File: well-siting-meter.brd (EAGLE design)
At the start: 93.8 x 65.9 mm, 46 parts, among them J2 7805, T1 MOSFET-NCHANNELFQP30N06L, U1 LCD-16X2NOHOLES, U2 ARDUINO_PRO_MINI, U3 EC2, U4 EC2, U5 AD623, U6 AD623, U7 MAX1771

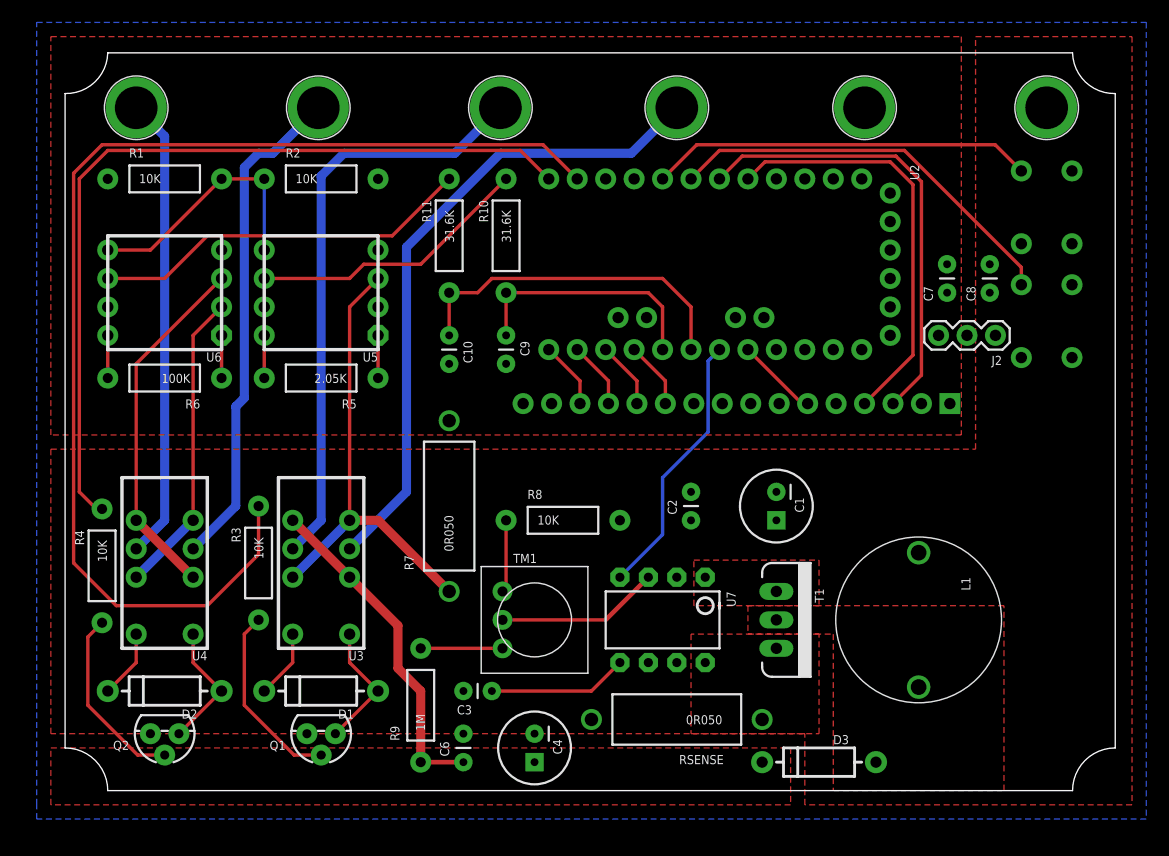
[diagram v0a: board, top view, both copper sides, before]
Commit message: adding optional 2nd inductor, more mfg prep
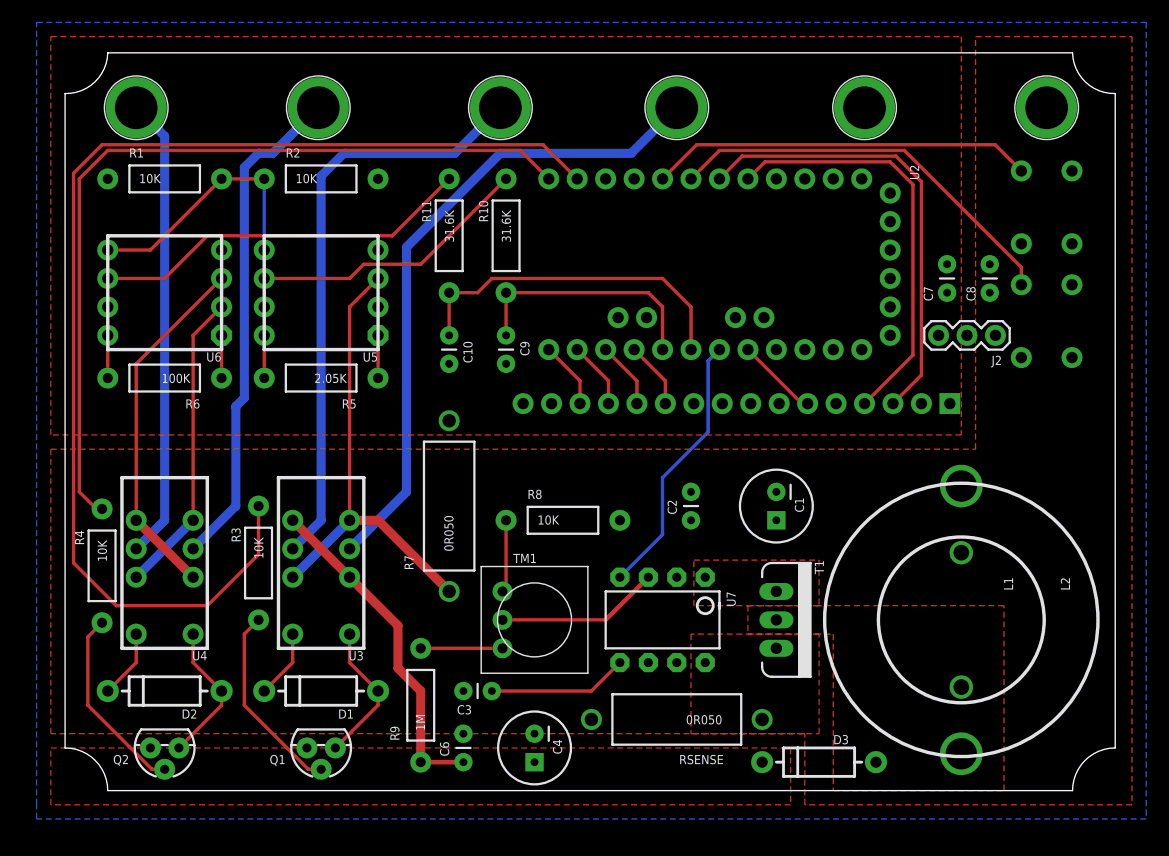
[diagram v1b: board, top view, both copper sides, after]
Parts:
- added L2: 47uH, murata1400:MURATA1400
- moved L1 3.81 mm to (81.3, 16.5)
- moved Q1 1.27 mm to (24.1, 5.08)
- moved Q2 1.27 mm to (10.2, 5.08)
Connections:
- net N$9: now also L2.P$2
- net V_BATT: now also L2.P$1
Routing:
- net N$4: track 11.5 -> 12.8 mm
- net N$1: track 11.5 -> 12.8 mm
- net N$5: track 16.8 -> 17.4 mm
- net N$2: track 16.6 -> 17.1 mm
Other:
- board text added: "BATT"
- board text added: "danwahl.github.io/"
- board text added: "rev -"
- board text added: "sn:"
- board text added: "v2"
- board text removed: "VBAT"
- board text removed: "danwahl.net/"
- board text removed: "v2 | rev - | sn:"
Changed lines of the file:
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@@
 <wire x1="91.2114" y1="1.27" x2="95.0214" y2="5.08" width="0" layer="20" curve="-90"/>
 <wire x1="1.27" y1="5.08" x2="5.08" y2="1.27" width="0" layer="20" curve="-90"/>
-<text x="93.98" y="14.478" size="1.778" layer="51" font="vector" ratio="10" rot="R90">well-siting-meter</text>
-<text x="74.93" y="2.54" size="0.8128" layer="51" font="vector" ratio="10">v2 | rev - | sn:</text>
-<text x="93.98" y="6.35" size="0.8128" layer="51" font="vector" ratio="10" rot="R90">danwahl.net/</text>
-<rectangle x1="86.36" y1="1.27" x2="91.44" y2="5.08" layer="51"/>
-<text x="88.9" y="66.04" size="1.016" layer="51" font="vector" ratio="10" align="center">VBAT</text>
+<text x="93.98" y="21.59" size="1.4224" layer="51" font="vector" ratio="10" rot="R90">well-siting-meter</text>
+<text x="83.82" y="29.21" size="0.8128" layer="51" font="vector" ratio="10" rot="R90">v2</text>
+<text x="91.44" y="25.146" size="0.8128" layer="51" font="vector" ratio="10" rot="R90">danwahl.github.io/</text>
+<text x="88.9" y="66.04" size="1.016" layer="51" font="vector" ratio="10" align="center">BATT</text>
 <text x="72.644" y="66.04" size="1.016" layer="51" font="vector" ratio="10" align="center">GND</text>
 <text x="55.88" y="66.04" size="1.016" layer="52" font="vector" ratio="10" rot="MR0" align="center">I1</text>
@@
 <text x="23.876" y="66.04" size="1.016" layer="51" font="vector" ratio="10" align="center">V1</text>
 <text x="7.62" y="66.04" size="1.016" layer="51" font="vector" ratio="10" align="center">V2</text>
-<text x="88.9" y="66.04" size="1.016" layer="52" font="vector" ratio="10" rot="MR0" align="center">VBAT</text>
+<text x="88.9" y="66.04" size="1.016" layer="52" font="vector" ratio="10" rot="MR0" align="center">BATT</text>
 <text x="72.644" y="66.04" size="1.016" layer="52" font="vector" ratio="10" rot="MR0" align="center">GND</text>
 <text x="55.88" y="66.04" size="1.016" layer="51" font="vector" ratio="10" align="center">I1</text>
@@
 <text x="23.876" y="66.04" size="1.016" layer="52" font="vector" ratio="10" rot="MR0" align="center">V1</text>
 <text x="7.62" y="66.04" size="1.016" layer="52" font="vector" ratio="10" rot="MR0" align="center">V2</text>
+<text x="86.36" y="28.448" size="0.8128" layer="51" font="vector" ratio="10" rot="R90">rev -</text>
+<text x="88.9" y="26.924" size="0.8128" layer="51" font="vector" ratio="10" rot="R90">sn:</text>
+<rectangle x1="87.376" y1="29.21" x2="89.916" y2="34.29" layer="51"/>
 </plain>
 <attributes>
@@
 <attribute name="VALUE" x="15.24" y="52.07" size="0.8128" layer="27" font="vector" rot="R180"/>
 </element>
-<element name="Q1" library="SparkFun-DiscreteSemi" package="TO-92" value="" x="24.13" y="6.35" smashed="yes" rot="R180">
-<attribute name="PROD_ID" value="TRANS-09536" x="24.13" y="6.35" size="1.778" layer="27" rot="R180" display="off"/>
-<attribute name="PN" value="PN2222AFS-ND" x="24.13" y="6.35" size="1.778" layer="27" rot="R180" display="off"/>
-<attribute name="NAME" x="20.955" y="5.715" size="0.8128" layer="25" font="vector" ratio="10" rot="R180"/>
-<attribute name="VALUE" x="20.955" y="7.62" size="0.4064" layer="27" ratio="10" rot="R180"/>
-</element>
-<element name="Q2" library="SparkFun-DiscreteSemi" package="TO-92" value="" x="10.16" y="6.35" smashed="yes" rot="R180">
-<attribute name="PROD_ID" value="TRANS-09536" x="10.16" y="6.35" size="1.778" layer="27" rot="R180" display="off"/>
-<attribute name="PN" value="PN2222AFS-ND" x="10.16" y="6.35" size="1.778" layer="27" rot="R180" display="off"/>
-<attribute name="NAME" x="6.985" y="5.715" size="0.8128" layer="25" font="vector" ratio="10" rot="R180"/>
-<attribute name="VALUE" x="6.985" y="7.62" size="0.4064" layer="27" ratio="10" rot="R180"/>
+<element name="Q1" library="SparkFun-DiscreteSemi" package="TO-92" value="" x="24.13" y="5.08" smashed="yes" rot="R180">
+<attribute name="PROD_ID" value="TRANS-09536" x="24.13" y="5.08" size="1.778" layer="27" rot="R180" display="off"/>
+<attribute name="PN" value="PN2222AFS-ND" x="24.13" y="5.08" size="1.778" layer="27" rot="R180" display="off"/>
+<attribute name="NAME" x="20.955" y="4.445" size="0.8128" layer="25" font="vector" ratio="10" rot="R180"/>
+<attribute name="VALUE" x="20.955" y="6.35" size="0.4064" layer="27" ratio="10" rot="R180"/>
+</element>
+<element name="Q2" library="SparkFun-DiscreteSemi" package="TO-92" value="" x="10.16" y="5.08" smashed="yes" rot="R180">
+<attribute name="PROD_ID" value="TRANS-09536" x="10.16" y="5.08" size="1.778" layer="27" rot="R180" display="off"/>
+<attribute name="PN" value="PN2222AFS-ND" x="10.16" y="5.08" size="1.778" layer="27" rot="R180" display="off"/>
+<attribute name="NAME" x="6.985" y="4.445" size="0.8128" layer="25" font="vector" ratio="10" rot="R180"/>
+<attribute name="VALUE" x="6.985" y="6.35" size="0.4064" layer="27" ratio="10" rot="R180"/>
 </element>
 <element name="D1" library="SparkFun-DiscreteSemi" package="DIODE-1N4001" value="" x="24.13" y="10.16" smashed="yes" rot="R180">
@@
 <attribute name="PN" value="BC2665CT-ND" x="39.37" y="10.16" size="1.778" layer="27" rot="R180" display="off"/>
 <attribute name="NAME" x="37.592" y="8.89" size="0.8128" layer="25" font="vector" rot="R180"/>
-<attribute name="VALUE" x="39.116" y="12.192" size="0.8128" layer="27" font="vector" rot="R180"/>
+<attribute name="VALUE" x="37.846" y="12.192" size="0.8128" layer="27" font="vector" rot="R180"/>
 </element>
 <element name="T1" library="SparkFun-DiscreteSemi" package="TO220V" value="MOSFET-NCHANNELFQP30N06L" x="64.77" y="16.51" smashed="yes" rot="R270">
 <attribute name="PROD_ID" value="TRANS-10060" x="64.77" y="16.51" size="1.778" layer="27" rot="R270" display="off"/>
 <attribute name="PN" value="FDP33N25-ND" x="64.77" y="16.51" size="1.778" layer="27" rot="R270" display="off"/>
-<attribute name="NAME" x="68.199" y="19.304" size="0.8128" layer="25" font="vector" ratio="10" rot="R270"/>
+<attribute name="NAME" x="68.199" y="21.844" size="0.8128" layer="25" font="vector" ratio="10" rot="R270"/>
 </element>
 <element name="D3" library="SparkFun-DiscreteSemi" package="DIODE-1N4001" value="" x="68.58" y="3.81" smashed="yes" rot="R180">
@@
 <attribute name="VALUE" x="41.275" y="10.16" size="1.27" layer="27"/>
 </element>
-<element name="L1" library="misc" package="1415" value="22uH" x="77.47" y="16.51" smashed="yes" rot="R270">
-<attribute name="NAME" x="81.28" y="20.32" size="0.8128" layer="25" font="vector" rot="R270"/>
-<attribute name="VALUE" x="72.39" y="20.32" size="0.8128" layer="27" font="vector" rot="R270"/>
+<element name="L1" library="misc" package="1415" value="22uH" x="81.28" y="16.51" smashed="yes" rot="R270">
+<attribute name="NAME" x="85.09" y="20.32" size="0.8128" layer="25" font="vector" rot="R270"/>
+<attribute name="VALUE" x="76.2" y="20.32" size="0.8128" layer="27" font="vector" rot="R270"/>
+<attribute name="PN" value="732-7163-ND" x="81.28" y="16.51" size="1.778" layer="27" rot="R270" display="off"/>
+</element>
+<element name="L2" library="murata1400" package="MURATA1400" value="47uH" x="81.28" y="16.51" smashed="yes" rot="R270">
+<attribute name="NAME" x="90.17" y="20.32" size="0.8128" layer="25" font="vector" ratio="10" rot="R270"/>
+<attribute name="VALUE" x="71.12" y="20.32" size="0.8128" layer="27" font="vector" ratio="10" rot="R270"/>
+<attribute name="PN" value="811-2633-ND" x="81.28" y="16.51" size="1.778" layer="27" rot="R270" display="off"/>
 </element>
 </elements>
@@
 <wire x1="15.24" y1="10.16" x2="12.7" y2="12.7" width="0.3048" layer="1"/>
 <wire x1="12.7" y1="12.7" x2="12.7" y2="15.24" width="0.3048" layer="1"/>
-<wire x1="11.43" y1="6.35" x2="15.24" y2="10.16" width="0.3048" layer="1"/>
+<wire x1="15.24" y1="10.16" x2="15.24" y2="8.89" width="0.3048" layer="1"/>
+<wire x1="15.24" y1="8.89" x2="11.43" y2="5.08" width="0.3048" layer="1"/>
 </signal>
 <signal name="N$2">
@@
 <wire x1="4.572" y1="16.256" x2="3.302" y2="14.986" width="0.3048" layer="1"/>
 <wire x1="3.302" y1="14.986" x2="3.302" y2="8.89" width="0.3048" layer="1"/>
-<wire x1="3.302" y1="8.89" x2="7.747" y2="4.445" width="0.3048" layer="1"/>
-<wire x1="7.747" y1="4.445" x2="10.16" y2="4.445" width="0.3048" layer="1"/>
+<wire x1="10.16" y1="3.175" x2="9.017" y2="3.175" width="0.3048" layer="1"/>
+<wire x1="9.017" y1="3.175" x2="3.302" y2="8.89" width="0.3048" layer="1"/>
 </signal>
 <signal name="VSW">
@@
 <wire x1="29.21" y1="10.16" x2="26.67" y2="12.7" width="0.3048" layer="1"/>
 <wire x1="26.67" y1="12.7" x2="26.67" y2="15.24" width="0.3048" layer="1"/>
-<wire x1="25.4" y1="6.35" x2="29.21" y2="10.16" width="0.3048" layer="1"/>
+<wire x1="29.21" y1="10.16" x2="29.21" y2="8.89" width="0.3048" layer="1"/>
+<wire x1="29.21" y1="8.89" x2="25.4" y2="5.08" width="0.3048" layer="1"/>
 </signal>
 <signal name="N$5">
@@
 <wire x1="18.542" y1="16.51" x2="17.272" y2="15.24" width="0.3048" layer="1"/>
 <wire x1="17.272" y1="15.24" x2="17.272" y2="8.89" width="0.3048" layer="1"/>
-<wire x1="17.272" y1="8.89" x2="21.717" y2="4.445" width="0.3048" layer="1"/>
-<wire x1="21.717" y1="4.445" x2="24.13" y2="4.445" width="0.3048" layer="1"/>
+<wire x1="24.13" y1="3.175" x2="22.987" y2="3.175" width="0.3048" layer="1"/>
+<wire x1="22.987" y1="3.175" x2="17.272" y2="8.89" width="0.3048" layer="1"/>
 </signal>
 <signal name="ISW">
@@
 <contactref element="C2" pad="1"/>
 <contactref element="L1" pad="P1"/>
+<contactref element="L2" pad="P$1"/>
 </signal>
 <signal name="RS">
@@
 </polygon>
 <contactref element="L1" pad="P2"/>
+<contactref element="L2" pad="P$2"/>
 </signal>
 <signal name="N$10">

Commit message: fixed cap packages (5mm)
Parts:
- C10, C2, C3, C6, C7, C8, C9: device SparkFun-Passives:CAP-PTH-SMALL -> SparkFun-Passives:CAP-PTH-5MM
- moved C3 3.81 mm to (43.2, 10.2)
- moved C6 2.54 mm to (36.8, 6.35)
- moved C7 2.54 mm to (80.0, 48.3)
- moved C8 2.54 mm to (83.8, 48.3)
- moved C2 1.27 mm to (57.1, 26.7)
- moved C10 1.27 mm to (35.6, 40.6)
- moved C9 1.27 mm to (40.6, 40.6)
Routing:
- net N$7: track 12.5 -> 6.17 mm
- net B1: track 36.4 -> 38.6 mm
- net VOUT: track 30.8 -> 29.6 mm
- net IOUT: track 22.1 -> 20.9 mm
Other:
- board text added: "rev A"
- board text removed: "rev -"

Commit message: rev A updates, arduino testing
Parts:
- C1, C4: device SparkFun-Passives:CPOL-RADIAL-100UF-25V -> SparkFun-Passives:CPOL-RADIAL-1000UF-25V
- R3, R4: value 10K -> 390
- U5, U6: device ad623:AD623 -> ad623:DIP08
- moved TM1 6.35 mm to (43.2, 22.9)
- moved C3 5.24 mm to (44.5, 15.2)
- moved R8 5.08 mm to (45.7, 30.5)
- moved RSENSE 3.94 mm to (59.7, 8.64)
- moved C4 2.84 mm to (44.5, 7.62)
- moved R5 2.54 mm to (24.1, 35.6)
- moved R6 2.54 mm to (10.2, 35.6)
- moved C7 1.27 mm to (80.0, 49.5)
- moved C8 1.27 mm to (83.8, 49.5)
- moved J2 1.27 mm to (84.3, 43.2)
- moved R1 1.27 mm to (10.2, 54.6)
- moved R2 1.27 mm to (24.1, 54.6)
- moved C6 1.27 mm to (36.8, 7.62)
- moved C1 1.27 mm to (64.8, 27.9)
- moved R9 1.27 mm to (33.0, 10.2)
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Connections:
- net GND: now also Q1.1, Q2.1; no longer Q1.3, Q2.3
- net N$1: now also Q2.3, U4.1; no longer Q2.1, U4.12
- net N$4: now also Q1.3, U3.1; no longer Q1.1, U3.12
- net V_BATT: now also U3.12, U4.12; no longer U3.1, U4.1
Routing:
- net VIN: track 30.1 -> 25.1 mm
- net V_BATT: track 12.3 -> 8.03 mm
- net N$27: track 3.81 -> 6.88 mm
- net N$26: track 3.81 -> 6.88 mm
- net N$25: track 3.81 -> 6.88 mm
- net N$24: track 3.81 -> 6.88 mm
- net VREF: track 23.0 -> 20.4 mm
- net N$6: track 7.30 -> 9.41 mm
- net N$15: track 14.6 -> 16.2 mm
- net N$7: track 6.17 -> 4.90 mm
- net N$8: track 6.48 -> 5.21 mm
- net N$14: track 34.2 -> 32.9 mm
- net N$12: track 25.3 -> 24.0 mm
- net IRET: track 41.3 -> 40.8 mm
- net V-: track 27.3 -> 26.8 mm
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
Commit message: rev A, bom updates
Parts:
- R3, R4: value 390 -> 392R
- RSENSE: value 0R050 -> 0R010
- moved C7 1.80 mm to (78.7, 48.3)
- moved S1 1.80 mm to (87.6, 41.9)
- moved S2 1.80 mm to (87.6, 52.1)
- moved C10 1.80 mm to (34.3, 39.4)
- moved C9 1.80 mm to (39.4, 39.4)
- moved R7 1.80 mm to (34.3, 25.4)
- moved J7 1.80 mm to (87.6, 61.0)
- moved J8 1.80 mm to (71.4, 61.0)
- moved T1 1.80 mm to (62.2, 15.2)
- moved C4 1.80 mm to (43.2, 6.35)
- moved C3 1.80 mm to (43.2, 14.0)
- moved R3 1.80 mm to (17.3, 20.3)
- moved R5 1.80 mm to (22.9, 34.3)
- moved R6 1.80 mm to (8.89, 34.3)
- moved R9 1.80 mm to (31.8, 8.89)
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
